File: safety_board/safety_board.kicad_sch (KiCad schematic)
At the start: 15 parts, among them J1 XT60-M, J2 XT60-M, K1 G5LE-14 DC5, K2 G5LE-14 DC5, U1 IRLML6344TRPBF, U1 SN74HC21DR, U2 LM358DT

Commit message: component selection
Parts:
- removed R?: R_US, symbol Device:R_US
- added C1: 470pF, SMV_Passives:CAPC17595_87N_KEM-M, symbol SMV_Custom:C0603C471J5GACTU
- added C2: 10μF, SMV_Passives:CAPC340270_190N_KEM-M, symbol Device:C
- added C3, C4, C?: 1 µF, SMV_Passives:CAPC340270_190N_KEM-M, symbol Device:C
- added CR? (x2): 1N4007-G, SMV_Passives:1N4-G, symbol SMV_Custom:1N4007-G
- added J1, J2, J3, J4: 430450200, CONN_SD-43045-001_02_MOL, symbol SMV_Custom:430450200
- added J1: 22035035, SMV_Connectors:3pin_CON_22035035_MOL, symbol SMV_Custom:3-pin Mini Molex Spox
- added J?: XT60-M, SMV_Connectors:AMASS_XT60-M, symbol SMV_Custom:XT60-M
- added K3, K?: G5LE-14 DC5, RELAY_G5LE-1 DC5_OMR, symbol SMV_Custom:G5LE-14_DC5
- added R? (x5): R_US, symbol Device:R_US
- added TP_5V1, TS_CAN_H1, TS_CAN_L1: ~, TestPoint:TestPoint_Pad_D2.5mm, symbol Connector:TestPoint
- added U1: MIC5219-5.0YM5-TR, SMV_ICs:SOT-23-5_MC_MCH, symbol SMV_Custom:MIC5219-5.0YM5-TR
- K1, K2: value G5LE-14 DC5 -> J115F11AH12VDCS61.5U; footprint SMV_ICs:RELAY_G5LE-1 DC5_OMR -> (none)
- gave numbers to parts that had none: 1
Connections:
- net +3V3: now also J1.2, J2.2, J3.2
- net +5V: now also C2.1, C3.1, C4.1, CR?.1, CR?.1, K3.1, K?.1, TP_5V1.1, U1.5 (OUT); no longer CR1.1, CR2.1, K1.1, K2.1
- net DRAIN: now also CR?.2, CR?.2, K3.2, K?.2
- net ESTOP1: now also J1.1, R?.1
- net ESTOP2: now also J2.1, R?.1
- net GND: now also RP2040.30 (GND), C1.2, C2.2, C3.2, C4.2, C?.2, J1.2, R?.1, R?.2, R?.2, R?.2, R?.2, U1.2 (GND)
- net HSENSE: now also J3.1, R?.1
- net IGNITION: now also RP2040.10 (D5), C?.1, R?.1
- net at U1.6 (1Y): now also U1.1 (G), R?.2
- net CAN_L: now reaches RP2040.29 (CAN_L)
- net CAN_L: now also J1.3, TS_CAN_L1.1
- net CAN_H: now reaches RP2040.31 (CAN_H)
- net CAN_H: now also J1.1, TS_CAN_H1.1
- new net: J?.N (NEG), K?.3
- new net: C1.1, U1.4 (BYP)
- new net: J?.P (POS), K3.3
- new net: J4.1, U1.1 (IN), U1.3 (EN)
- new net +12V: CR1.1, CR2.1, J4.2, K1.1, K2.1
- new net HFC: K3.4, K?.4
- no-connect marks 4 -> 26
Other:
- moved on the sheet: J1, U2

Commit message: formatting
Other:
- note added: "HFC Relays"
- note added: "LDO 12V->5V"
- note added: "Power Relays"
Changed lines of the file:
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@@
+	)
+	(rectangle
+		(start 75.565 13.335)
+		(end 212.725 66.675)
+		(stroke
+			(width 0)
+			(type default)
+		)
+		(fill
+			(type none)
+		)
+	)
+	(rectangle
+		(start 163.83 69.215)
+		(end 283.845 107.95)
+		(stroke
+			(width 0)
+			(type default)
+		)
+		(fill
+			(type none)
+		)
 	)
 	(rectangle
@@
 		)
 	)
+	(rectangle
+		(start 13.335 13.335)
+		(end 73.025 66.675)
+		(stroke
+			(width 0)
+			(type default)
+		)
+		(fill
+			(type none)
+		)
+	)
 	(text "AND GATE INPUTS\n"
 		(exclude_from_sim no)
 		(at 25.654 117.856 0)
+		(effects
+			(font
+				(size 1.27 1.27)
+			)
+		)
+	)
+	(text "LDO 12V->5V\n"
+		(exclude_from_sim no)
+		(at 172.212 71.628 0)
+		(effects
+			(font
+				(size 1.27 1.27)
+			)
+		)
+	)
+	(text "Power Relays\n"
+		(exclude_from_sim no)
+		(at 82.296 15.748 0)
 		(effects
 			(font
@@
 		(effects
 			(font
+				(size 1.27 1.27)
+			)
+		)
+	)
+	(text "HFC Relays\n"
+		(exclude_from_sim no)
+		(at 19.558 14.986 0)
+		(effects
+			(font

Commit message: schematic updates
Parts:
- removed C3: 1 µF, SMV_Passives:CAPC340270_190N_KEM-M, symbol Device:C
- removed CR? (x2): 1N4007-G, SMV_Passives:1N4-G, symbol SMV_Custom:1N4007-G
- removed K1, K2: J115F11AH12VDCS61.5U, symbol SMV_Custom:G5LE-14_DC5
- removed K3: G5LE-14 DC5, RELAY_G5LE-1 DC5_OMR, symbol SMV_Custom:G5LE-14_DC5
- removed U1: SN74HC21DR, D14, symbol SMV_Custom:SN74HC21DR
- added C?: 1 µF, SMV_Passives:CAPC340270_190N_KEM-M, symbol Device:C
- added CR1: 5KP48A, DIODE_P600_VIS, symbol SMV_Custom:5KP48A
- added F1: 3555-2, 3555-2:FUSE_3555-2, symbol SMV_Custom:3555-2
- added R3: 10k ohms, symbol Device:R_US
- added U2: SN74HCS21QPWRQ1, SMV_ICs:TSSOP14_PW_TEX-M, symbol SMV_Custom:SN74HCS21QPWRQ1
- added U3: ISL21080CIH315Z-TK, SMT_330Z-TK_REN, symbol SMV_Custom:ISL21080CIH315Z-TK
- added U5, U6: J115F11AH12VDCS61.5U, symbol SMV_Custom:J115F11AH12VDCS61.5U
- R1, R2, R4, R6, R7: renamed from R?; value R_US -> 10k ohms
- gave numbers to parts that had none: 2
- renumbered C2 to C3, C1 to C5, R1 to R5, U1 to U4
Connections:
- net +12V: now also U5. (4), U6. (4)
- net +1V5: now also U3.2 (VOUT)
- net +5V: now also C?.1, U2.14 (VCC), U3.1 (VIN)
- net DRAIN: now also U6. (4); no longer K1.2
- net ESTOP1: now also U2.2 (1B)
- net ESTOP2: now also U2.4 (1C)
- net GND: now also C?.2, CR1.2, U2.10 (2B), U2.12 (2C), U2.13 (2D), U2.7 (GND), U2.9 (2A), U3.3 (GND)
- net HFC: now also K1.5; no longer K1.4
- net HSENSE_INVERT: now also U2.1 (1A)
- net IGNITION: now also U2.5 (1D)
- net at J1.P (POS): now also F1.1_1
- net at J2.P (POS): now also U5. (4)
- net at R4.2, U1.1 (G): now also R3.2
- net at J2.N (NEG): now also U6. (4)
- net at J1.N (NEG): now also U6. (4)
- net at J?.P (POS): now also K1.2
- new net: CR1.1, F1.2_1, U5. (4)
- new net: R3.1, U2.6 (1Y)
- no-connect marks 26 -> 23
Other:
- note added: "HFC Relay"
- note removed: "HFC Relays"
- moved on the sheet: CR1, R4

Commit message: updates to schematic
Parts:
- added U2: IRLML6344TRPBF, SMV_ICs:IRLML6344TRPBF_INF-L, symbol SMV_Custom:IRLML6344TRPBF
- gave numbers to parts that had none: 1
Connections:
- net +5V: now also K1.5; no longer K1.1
- net DRAIN: now also U5. (4); no longer CR2.2, U6. (4)
- net GND: now also U2.2 (S)
- net HFC: now also K1.4; no longer K1.5
- net at R3.2, R4.2, U1.1 (G): now also U2.1 (G)
- new net DRAIN2: CR2.2, U2.3 (D), U6. (4)
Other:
- moved on the sheet: U1

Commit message: schematic changes
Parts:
- removed C3: 10μF, SMV_Passives:CAPC340270_190N_KEM-M, symbol Device:C
- removed C5: 470pF, SMV_Passives:CAPC17595_87N_KEM-M, symbol SMV_Custom:C0603C471J5GACTU
- removed U2: IRLML6344TRPBF, SMV_ICs:IRLML6344TRPBF_INF-L, symbol SMV_Custom:IRLML6344TRPBF
- removed U4: MIC5219-5.0YM5-TR, SMV_ICs:SOT-23-5_MC_MCH, symbol SMV_Custom:MIC5219-5.0YM5-TR
- added C3: C0603C474K4RACTU, SMV_Passives:CAPC17595_87N_KEM-L, symbol SMV_Custom:C0603C474K4RACTU
- added C4: C0402C104K4RACTU, SMV_Passives:CAPC1005X55N, symbol SMV_Custom:C0402C104K4RACTU
- added CR3: 5KP48A, DIODE_P600_VIS, symbol SMV_Custom:5KP48A
- added CR4, CR5, CR6: 1N4007-G, SMV_Passives:1N4-G, symbol SMV_Custom:1N4007-G
- added F2: 3555-2, 3555-2:FUSE_3555-2, symbol SMV_Custom:3555-2
- added J?: XT60-M, SMV_Connectors:AMASS_XT60-M, symbol SMV_Custom:XT60-M
- added R?: R_US, symbol Device:R_US
- added U?: UA78M05QDCYRG4Q1, SMV_ICs:DCY4_TEX, symbol SMV_Custom:UA78M05QDCYRG4Q1
- added U? (x3): J115F11AH12VDCS61.5U, symbol SMV_Custom:J115F11AH12VDCS61.5U
- renumbered CR1 to CR7, CR2 to CR8
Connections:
- net DRAIN2 is gone; now on net DRAIN: CR8.2, U6. (4)
- net +12V: now also CR4.1, CR5.1, CR6.1, U?. (4), U?. (4), U?. (4)
- net +5V: now also C4.1, U?.3 (OUTPUT)
- net DRAIN: now also CR4.2, CR5.2, CR6.2, U?. (4), U?. (4), U?. (4)
- net GND: now also C3.2, C4.2, CR3.2, U?.2 (GND), U?.4 (GND)
- net at J1.N (NEG), U6. (4): now also U?. (4)
- net at CR1.1, F1.2_1, U5. (4): now also R?.2, U?. (4)
- net at J4.1: now also C3.1, U?.1 (INPUT)
- new net: J?.N (NEG), U?. (4)
- new net: CR3.1, F2.2_1, J?.P (POS)
- new net: F2.1_1, U?. (4), U?. (4)
- new net: R?.1, U?. (4)
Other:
- note added: "check fuses in shop"
- note added: "update this with shop relays"
- moved on the sheet: CR1, CR7, CR8, F1, J1, J2, U1, U5, U6

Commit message: schematic updates
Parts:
- removed CR1: 5KP48A, DIODE_P600_VIS, symbol SMV_Custom:5KP48A
- removed K1: G5LE-14 DC5, RELAY_G5LE-1 DC5_OMR, symbol SMV_Custom:G5LE-14_DC5
- removed U3: ISL21080CIH315Z-TK, SMT_330Z-TK_REN, symbol SMV_Custom:ISL21080CIH315Z-TK
- added CR?: 1N4007-G, SMV_Passives:1N4-G, symbol SMV_Custom:1N4007-G
- added D1, D2: SMA4S56AH, SMA4S56AH:SODFL4725X110N, symbol SMV_Custom:SMA4S56AH
- added F2: 3555-2, 3555-2:FUSE_3555-2, symbol SMV_Custom:3555-2
- added R8: CRCW060310K0FKEA, CRCW060310K0FKEA:RESC1508X50N, symbol SMV_Custom:CRCW060310K0FKEA
- added R9: TC33X-2-104E, SMV_Passives:TRIM_TC33X-2-104E, symbol SMV_Custom:TC33X-2-104E
- added TP_12V: ~, TestPoint:TestPoint_Pad_D2.5mm, symbol Connector:TestPoint
- added TP_48V, TP_VDIVIDER: V_DIVIDED, symbol Connector:TestPoint
- added U?: J115F11AH12VDCS61.5U, symbol SMV_Custom:J115F11AH12VDCS61.5U
- gave numbers to parts that had none: 1
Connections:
- net +12V: now also CR?.1, TP_12V.1, U?. (4)
- net +3V3: no longer J1.2, J2.2
- net +5V: now also J1.2, J2.2, R8.1
- net DRAIN: now also CR?.2, U?. (4)
- net GND: now also D1.A, D2.A, R9.3
- net at J?.P (POS): now also U?. (4)
- net at J?.N (NEG): now also U?. (4)
- net at F1.1_1, J1.P (POS): now also TP_48V.1
- net at F1.2_1, R?.2, U5. (4)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: now also D1.C
- net +1V5 renamed V_DIVIDED
- net V_DIVIDED: now also R8.2, R9.2, TP_VDIVIDER.1
- new net: D2.C, F2.2_1, U6. (4), U?. (4)
- new net: F2.1_1, J1.N (NEG)
- new net: F2.1_1, U?. (4), U?. (4)
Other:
- note removed: "check fuses in shop"
- note removed: "update this with shop relays"

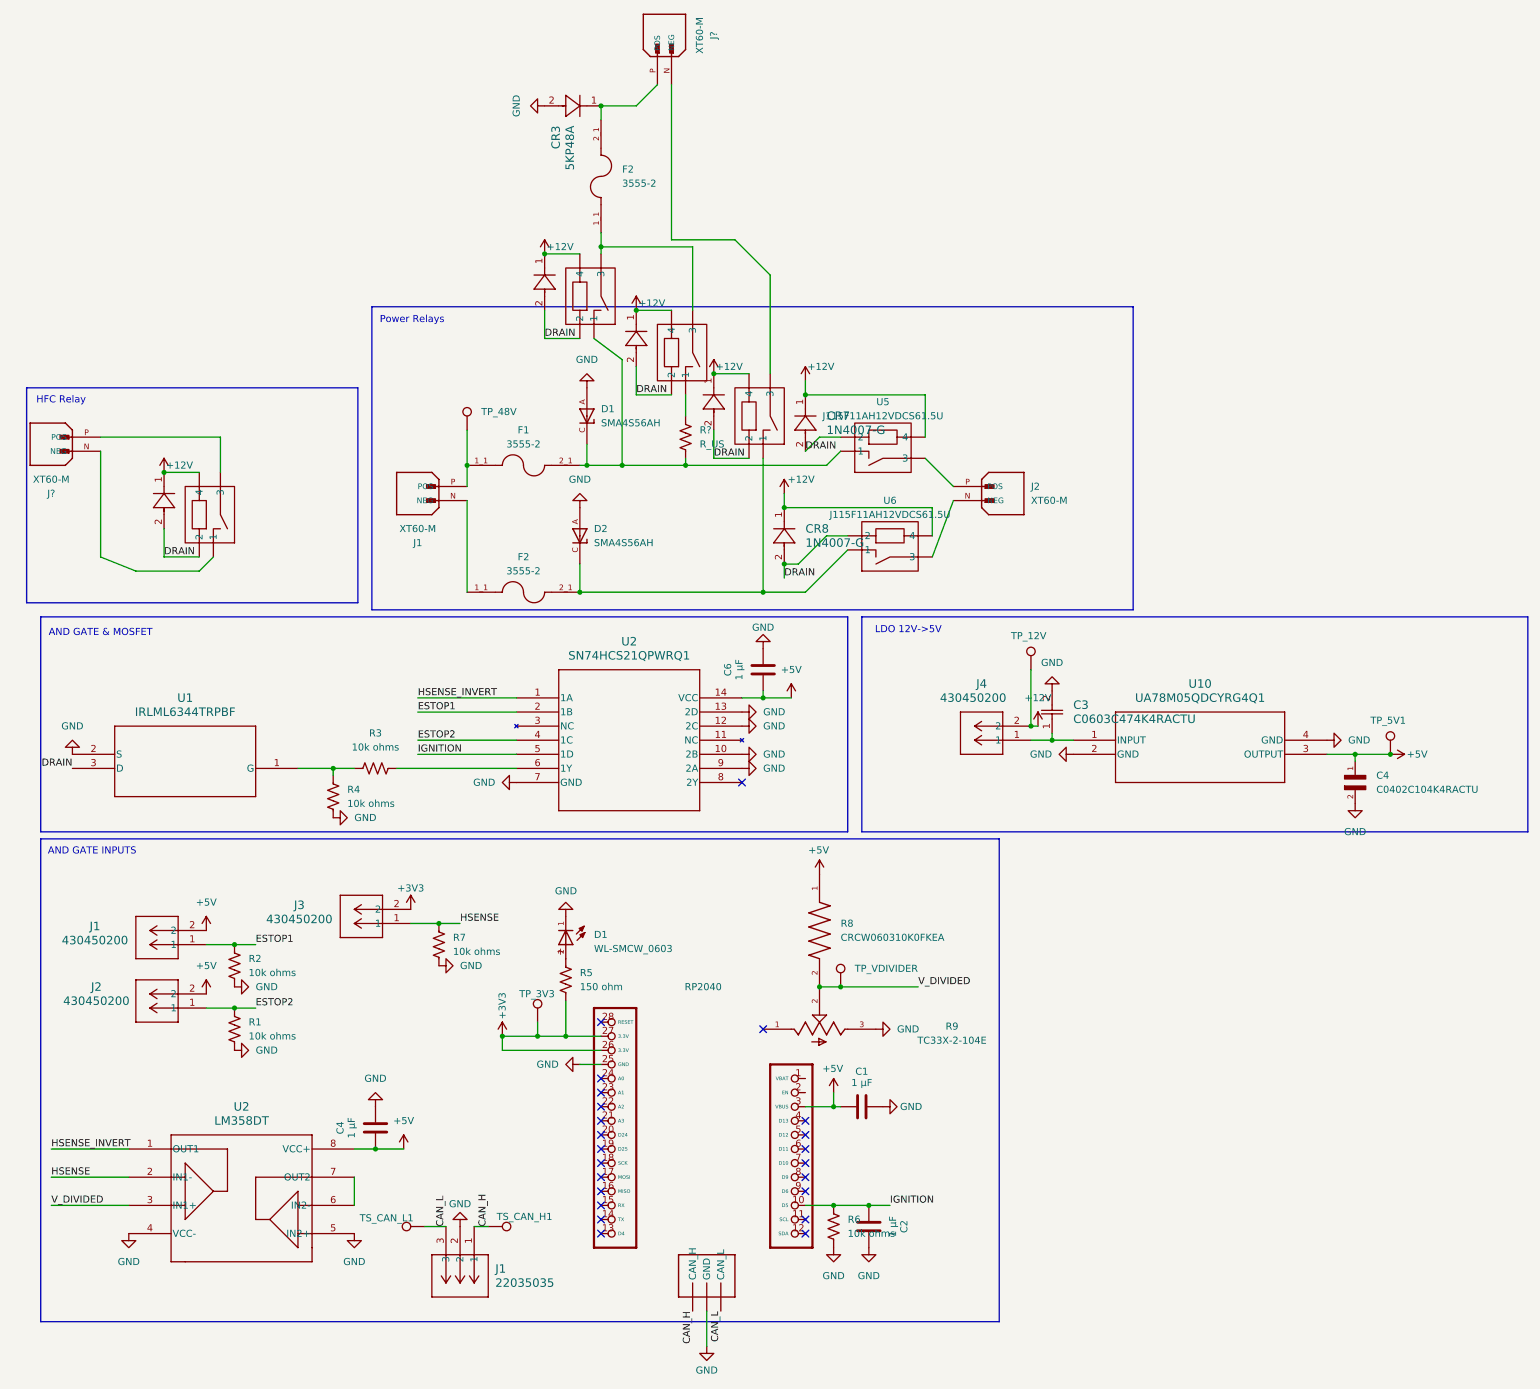
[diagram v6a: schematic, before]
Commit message: 4 hydrogen sensors
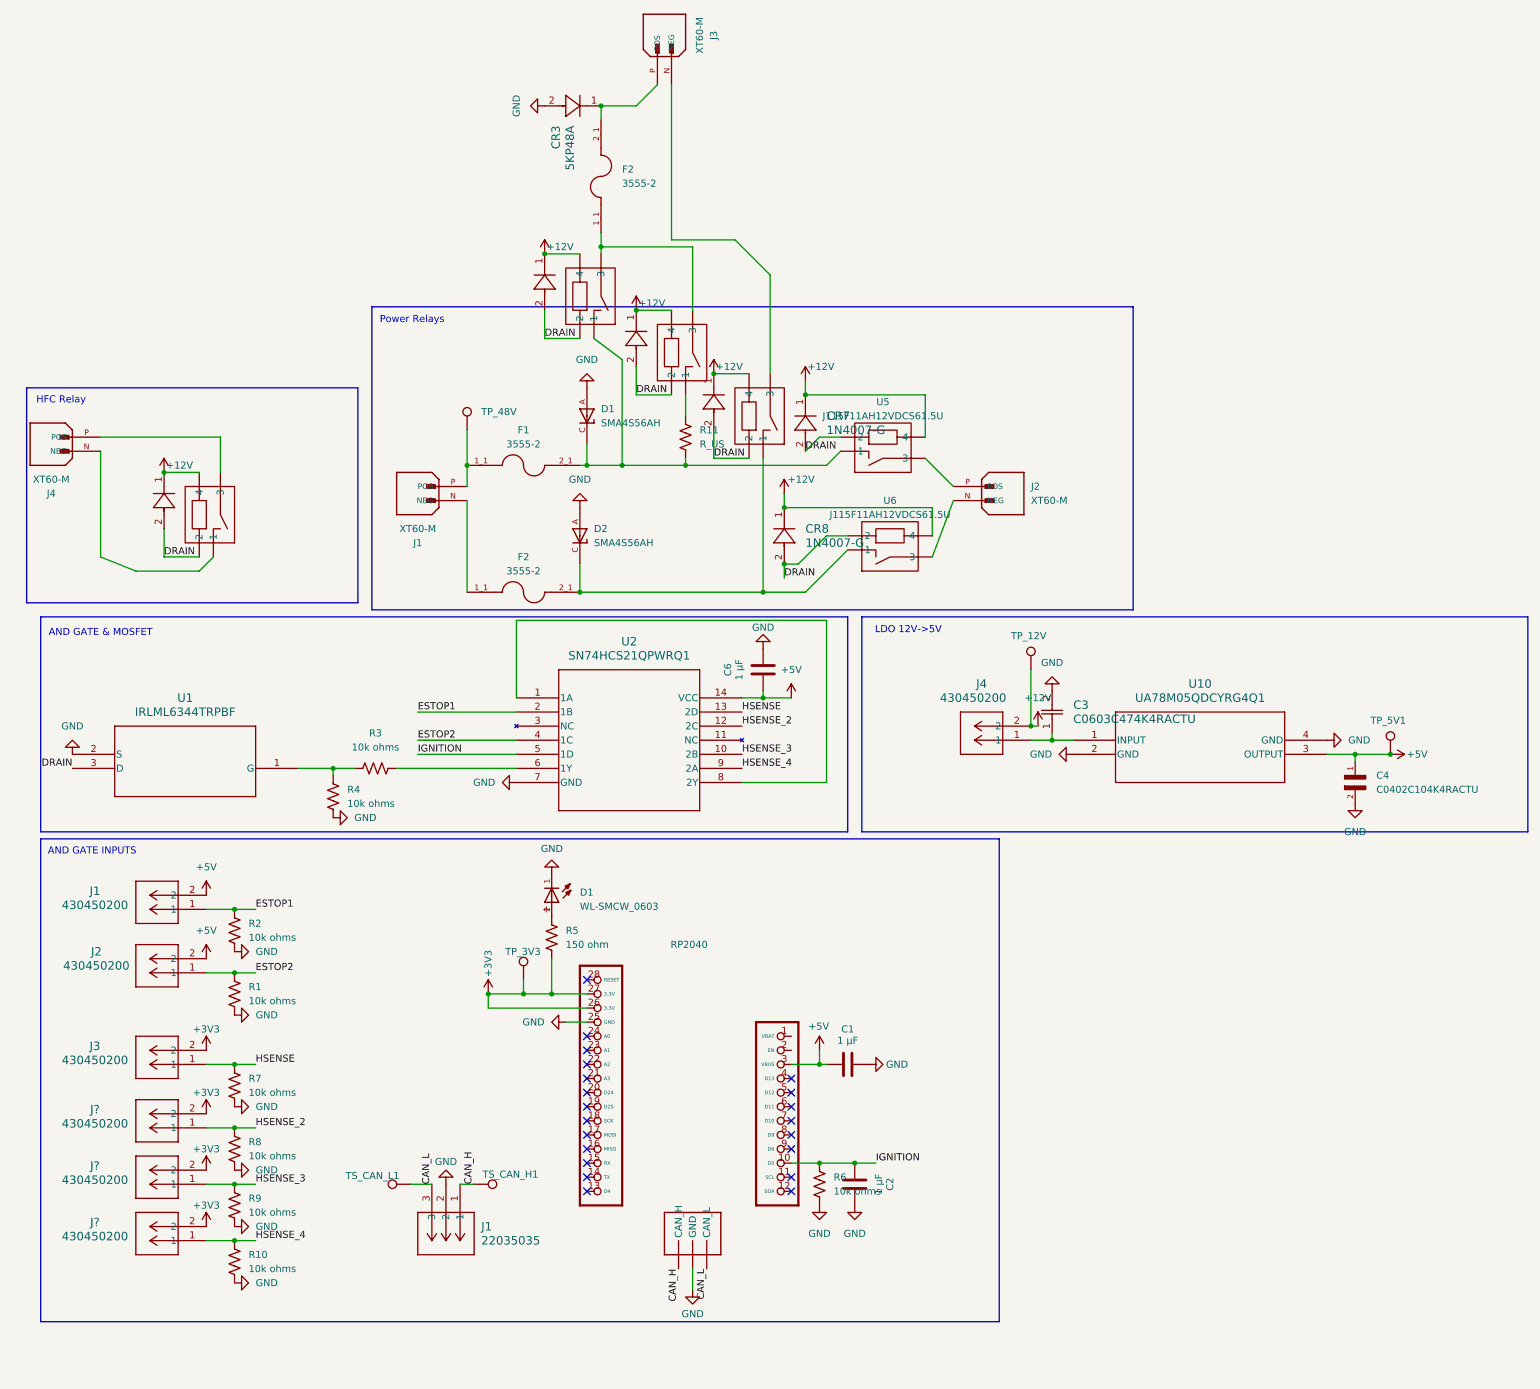
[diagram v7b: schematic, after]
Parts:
- removed C4: 1 µF, SMV_Passives:CAPC340270_190N_KEM-M, symbol Device:C
- removed R8: CRCW060310K0FKEA, CRCW060310K0FKEA:RESC1508X50N, symbol SMV_Custom:CRCW060310K0FKEA
- removed R9: TC33X-2-104E, SMV_Passives:TRIM_TC33X-2-104E, symbol SMV_Custom:TC33X-2-104E
- removed TP_VDIVIDER: V_DIVIDED, symbol Connector:TestPoint
- removed U2: LM358DT, SO_358DT_STM, symbol SMV_Custom:LM358DT
- added J? (x3): 430450200, CONN_SD-43045-001_02_MOL, symbol SMV_Custom:430450200
- added R10, R8, R9: 10k ohms, symbol Device:R_US
- gave numbers to parts that had none: 3
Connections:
- net HSENSE_INVERT is gone; now on an unnamed net: U2.1 (1A)
- net +3V3: now also J?.2, J?.2, J?.2
- net GND: now also R10.2, R8.2, R9.2; no longer U2.10 (2B), U2.12 (2C), U2.13 (2D), U2.9 (2A)
- net HSENSE: now also U2.13 (2D)
- new net: F2.1_1, U?. (4), U?. (4)
- new net HSENSE_2: J?.1, R8.1, U2.12 (2C)
- new net HSENSE_3: J?.1, R9.1, U2.10 (2B)
- new net HSENSE_4: J?.1, R10.1, U2.9 (2A)
- no-connect marks 23 -> 21
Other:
- moved on the sheet: C1, C2, D1, J1, J2, J3, R1, R2, R5, R6, R7, RP2040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

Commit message: schematic
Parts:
- removed C4: C0402C104K4RACTU, SMV_Passives:CAPC1005X55N, symbol SMV_Custom:C0402C104K4RACTU
- removed CR5: 1N4007-G, SMV_Passives:1N4-G, symbol SMV_Custom:1N4007-G
- removed D2: SMA4S56AH, SMA4S56AH:SODFL4725X110N, symbol SMV_Custom:SMA4S56AH
- removed J3, J? (x3): 430450200, CONN_SD-43045-001_02_MOL, symbol SMV_Custom:430450200
- removed U10: UA78M05QDCYRG4Q1, SMV_ICs:DCY4_TEX, symbol SMV_Custom:UA78M05QDCYRG4Q1
- removed U?: J115F11AH12VDCS61.5U, symbol SMV_Custom:J115F11AH12VDCS61.5U
- added C?: C0402C104K4RACTU, SMV_Passives:CAPC1005X55N, symbol SMV_Custom:C0402C104K4RACTU
- added F4: 3555-2, 3555-2:FUSE_3555-2, symbol SMV_Custom:3555-2
- added J3, J4, J5, J6, J8: 22035035, SMV_Connectors:3pin_CON_22035035_MOL, symbol SMV_Custom:3-pin Mini Molex Spox
- added R12, R13: 10k ohms, symbol Device:R_US
- added R?: CRCW060310K0FKEA, CRCW060310K0FKEA:RESC1508X50N, symbol SMV_Custom:CRCW060310K0FKEA
- added R?: TC33X-2-104E, SMV_Passives:TRIM_TC33X-2-104E, symbol SMV_Custom:TC33X-2-104E
- added TP_VDIVIDER?: V_DIVIDED, symbol Connector:TestPoint
- added U1: LDL1117S50R, SMV_ICs:SOT223_STM, symbol SMV_Custom:LDL1117S50R
- added U3: MCP6286T-E/OT, SMV_ICs:SOT-23-5_MC_MCH, symbol SMV_Custom:MCP6286T-E_OT
- added U4: IRLML6344TRPBF, SMV_ICs:IRLML6344TRPBF_INF-L, symbol SMV_Custom:IRLML6344TRPBF
- R11: value R_US -> 10k ohms
- renumbered F2 to F3, J1 to J7
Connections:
- net +5V: now also C?.1, J3.1, J4.1, J5.1, J6.1, R?.1, U1.2 (VOUT), U1.4 (VOUT), U3.5 (VDD)
- net CAN_H: now also J8.1
- net CAN_L: now also J8.3
- net DRAIN: no longer CR4.2, U?. (4)
- net GND: now also R11.2, C?.2, J3.3, J4.3, J5.3, J6.3, J8.2, R12.1, R?.3, U1.1 (GND), U3.2 (VSS), U3.4 (VIN-), U4.2 (S)
- net HSENSE: now also J3.2
- net HSENSE_2: now also J4.2
- net HSENSE_3: now also J5.2
- net HSENSE_4: now also J6.2
- net IGNITION: now also R11.1, U3.3 (VIN+); no longer U2.5 (1D)
- net at C3.1, J4.1: now also U1.3 (VIN)
- net at CR3.1, F3.2_1, J3.P (POS): now also F4.2_1
- net at RP2040.6 (D11): now also R13.2
- net at J1.N (NEG): now also U6. (4), U?. (4); no longer F2.1_1
- net at F1.1_1, J1.P (POS), TP_48V.1: now also F2.1_1
- net at F3.1_1, U?. (4): now also F4.1_1
- new net: R12.2, R13.1, U4.1 (G)
- new net: D1.C, F1.2_1, F2.2_1, U5. (4), U?. (4)
- new net DRAIN2: CR4.2, U4.3 (D), U?. (4)
- new net IGNITION_5V: U2.5 (1D), U3.1 (VOUT)
- new net V_DIVIDED: R?.2, R?.2, TP_VDIVIDER?.1
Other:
- moved on the sheet: C3, D1, F1, F2, J4, R10, R7, R9, TP_12V
